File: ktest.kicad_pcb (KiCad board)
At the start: 2 copper layers, 16.3 x 14.2 mm, 2 parts

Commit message: add r1 c1 vlaue
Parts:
- C1: value C -> 10n
- R1: value R -> 10k
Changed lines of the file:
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@@
 		(capping no)
 		(filling no)
-		(zone_defaults)
 		(pcbplotparams
 			(layerselection 0x00000000_00000000_55555555_5755f5ff)
@@
 			)
 		)
-		(property "Value" "R"
+		(property "Value" "10k"
 			(at 0 1 0)
 			(layer "F.Fab")
@@
 			)
 		)
-		(property "Value" "C"
+		(property "Value" "10n"
 			(at 0 3.7 0)
 			(layer "F.Fab")

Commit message: added holes
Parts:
- R1: moved to B.Cu
- moved R1 0.95 mm to (128.4, 88.1)
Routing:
- net Net-(C1-Pad1): track 4.83 -> 5.78 mm, vias 0 -> 1
- net Net-(C1-Pad2): track 7.06 -> 7.46 mm, vias 0 -> 1

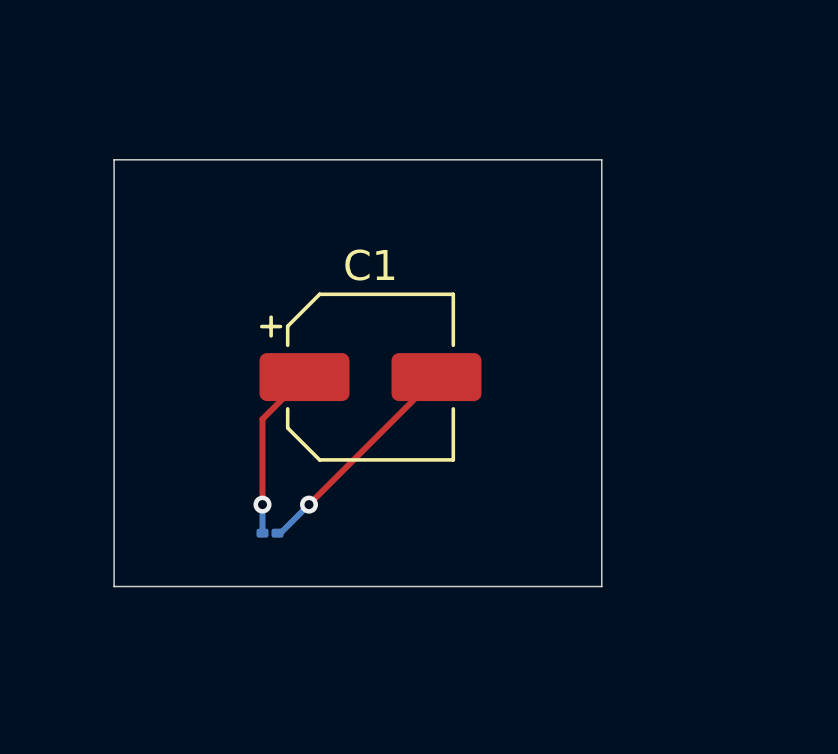
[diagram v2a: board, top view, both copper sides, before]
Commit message: 4 layers
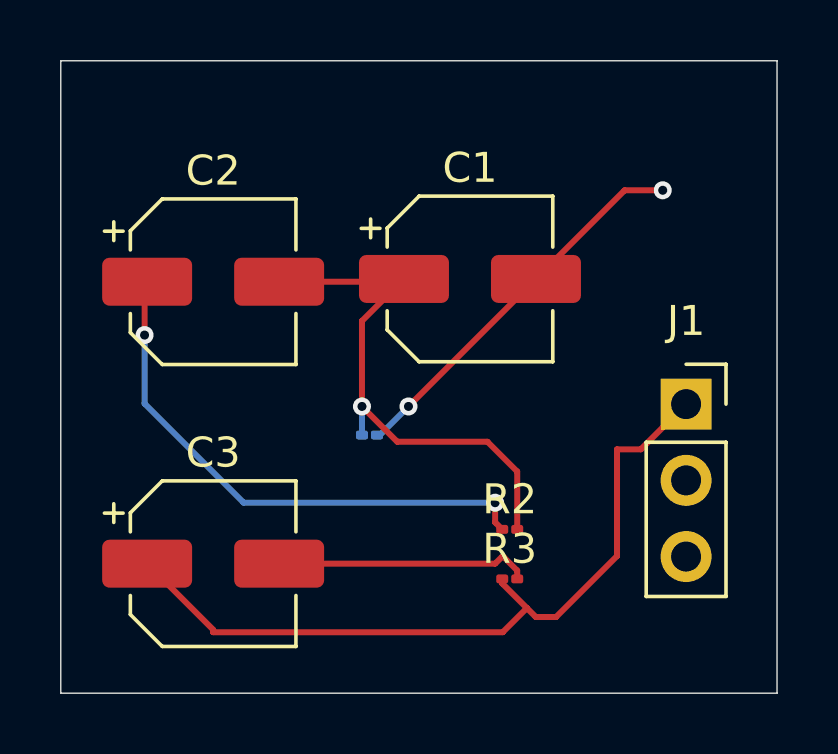
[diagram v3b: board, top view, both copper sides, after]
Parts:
- added C2: 10n, Capacitor_SMD:CP_Elec_5x5.9, F.Cu at (126.5, 79.8)
- added C3: 10n, Capacitor_SMD:CP_Elec_5x5.9, F.Cu at (126.5, 89.2)
- added J1: Conn_01x03_Pin, Connector_PinSocket_2.54mm:PinSocket_1x03_P2.54mm_Vertical, F.Cu at (142.3, 83.8)
- added R2: 10k, Resistor_SMD:R_01005_0402Metric, F.Cu at (136.4, 88.0)
- added R3: 10k, Resistor_SMD:R_01005_0402Metric, F.Cu at (136.4, 89.7)
- moved C1 4.66 mm to (135.1, 79.7)
- moved R1 4.66 mm to (131.7, 84.9)
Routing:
- net Net-(J1-Pin_1): track 0.00 -> 25.8 mm
- net Net-(J1-Pin_3): track 0.00 -> 25.3 mm, vias 0 -> 2
- net Net-(J1-Pin_2): track 7.46 -> 25.4 mm, vias 1 -> 2
- net Net-(C1-Pad1): track 5.78 -> 18.0 mm
- net Net-(C3-Pad2): track 0.00 -> 8.52 mm
- added copper zone on In2.Cu, net Net-(J1-Pin_3)
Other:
- board size 16.3 x 14.2 mm -> 23.9 x 21.1 mm
- copper layers 2 -> 4

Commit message: Keep local changes
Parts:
- moved C2 41.0 mm to (97.5, 50.8)
- moved J1 41.0 mm to (113.3, 54.9)
- moved R1 41.0 mm to (102.7, 55.9)
- moved R2 41.0 mm to (107.4, 59.1)
- moved R3 41.0 mm to (107.4, 60.7)
- moved C3 41.0 mm to (97.5, 60.2)
- moved C1 41.0 mm to (106.1, 50.7)

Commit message: pdf assy image
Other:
- board text added: "angled bottom render"
- board text added: "angled top render"
- board text added: "bottom render"
- board text added: "top render"
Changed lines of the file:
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@@
 		(43 "User.3" user)
 		(45 "User.4" user)
+		(47 "User.5" user "AssemblyOverview")
+		(49 "User.6" user "AssemblyTop")
+		(51 "User.7" user "AssemblyBottom")
+		(53 "User.8" user)
 	)
 	(setup
@@
 		(capping no)
 		(filling no)
+		(zone_defaults)
 		(pcbplotparams
 			(layerselection 0x00000000_00000000_55555555_5755f5ff)
@@
 		(layer "Edge.Cuts")
 	)
+	(gr_rect
+		(start 40.132 39.624)
+		(end 77.724 75.946)
+		(stroke
+			(width 0.1)
+			(type default)
+		)
+		(fill no)
+		(layer "User.5")
+	)
+	(gr_rect
+		(start 126.746 40.005)
+		(end 164.338 76.327)
+		(stroke
+			(width 0.1)
+			(type default)
+		)
+		(fill no)
+		(layer "User.5")
+	)
+	(gr_rect
+		(start 139.954 51.054)
+		(end 174.752 85.598)
+		(stroke
+			(width 0.1)
+			(type default)
+		)
+		(fill no)
+		(layer "User.6")
+	)
+	(gr_rect
+		(start 133.096 36.322)
+		(end 161.29 68.072)
+		(stroke
+			(width 0.1)
+			(type default)
+		)
+		(fill no)
+		(layer "User.7")
+	)
+	(gr_text "angled top render"
+		(at 58.674 42.926 0)
+		(layer "User.5")
+		(effects
+			(font
+				(size 1 1)
+				(thickness 0.15)
+			)
+			(justify bottom)
+		)
+	)
+	(gr_text "angled bottom render"
+		(at 145.288 43.307 0)
+		(layer "User.5")
+		(effects
+			(font
+				(size 1 1)
+				(thickness 0.15)
+			)
+			(justify bottom)
+		)
+	)
+	(gr_text "top render"
+		(at 153.924 53.594 0)
+		(layer "User.6")
+		(effects
+			(font
+				(size 1 1)
+				(thickness 0.15)
+			)
+			(justify left bottom)
+		)
+	)
+	(gr_text "bottom render"
+		(at 141.986 38.862 0)
+		(layer "User.7")
+		(effects
+			(font
+				(size 1 1)
+				(thickness 0.15)
+			)
+			(justify left bottom)
+		)
+	)
 	(segment
 		(start 106.892 58.819)
@@
 		)
 	)
+	(group "kibot_image_blender_angled_bottom"
+		(members "47a33e86-0a7b-4fb2-9f1a-8c1f9bbd8aef" "e0f4d6b7-6642-4f52-86d4-2c7661283d27")
+	)
+	(group "kibot_image_blender_angled_top"
+		(members "aadaafd9-59d6-406c-9e50-c65a85ec2e7b" "d245d129-484e-4480-aa49-d9efff5859e8")
+	)
+	(group "kibot_image_blender_top"
+		(members "3748c16f-f86b-4ed3-95e1-1cd301faa602" "54584b5a-66d1-40a4-a952-5988b66ec816")
+	)
+	(group "kibot_image_blender_bottom"
+		(members "60365628-61de-4015-826d-ef046bea2621" "ef773150-5c25-4b16-be8e-16da88ff3160")
+	)
 	(embedded_fonts no)
